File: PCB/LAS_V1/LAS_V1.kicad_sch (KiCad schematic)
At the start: 19 parts, among them J1 Screw_Terminal_01x04, J2 Conn_01x03_Pin, J3 Conn_01x05_Socket, J4 Conn_01x22_Socket, J5 Conn_01x22_Socket, SW1 SW_Push, SW2 SW_Push, U1 ESP32-S3-WROOM-1, U2 AMS1117-3.3

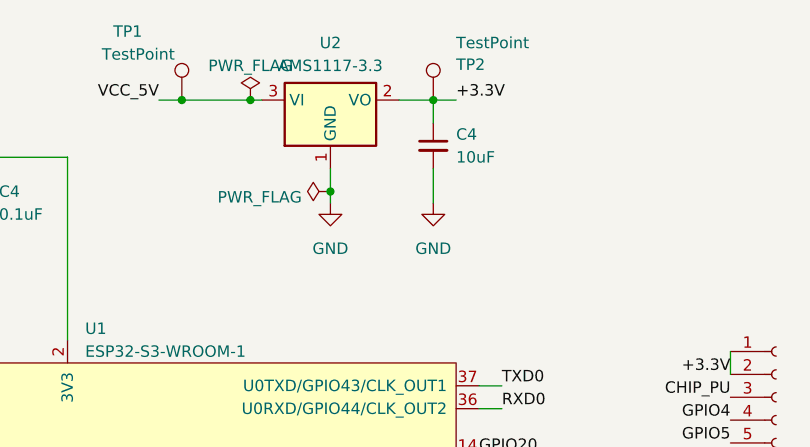
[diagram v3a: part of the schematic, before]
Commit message: All components Placed on PCB
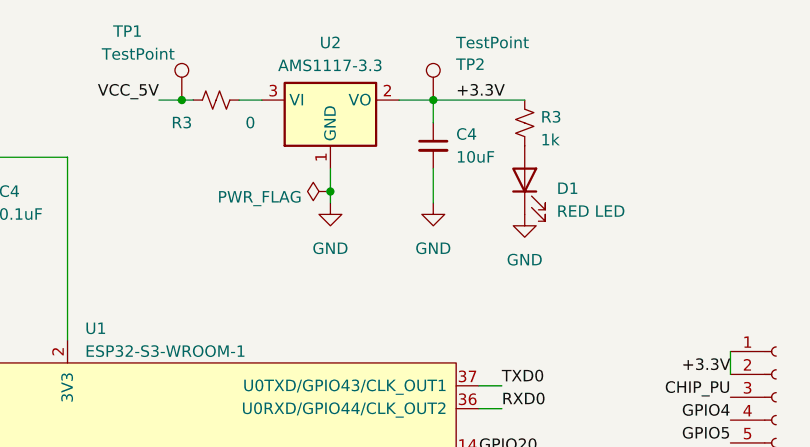
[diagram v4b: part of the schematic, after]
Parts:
- added D1: RED LED, LED_SMD:LED_0805_2012Metric, symbol Device:LED
- added R3: 1k, Resistor_SMD:R_0603_1608Metric, symbol Device:R_Small_US
- added R3: 0, Resistor_SMD:R_0603_1608Metric, symbol Device:R_Small_US
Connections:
- net +3.3V: now also R3.1
- net GND: now also D1.1 (K)
- net VCC_5V: now also R3.2; no longer U2.3 (VI)
- new net: D1.2 (A), R3.2
- new net: R3.1, U2.3 (VI)
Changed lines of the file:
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@@
   (junction (at 180.34 31.75) (diameter 0) (color 0 0 0 0)
-  )
-  (junction (at 210.82 25.4) (diameter 0) (color 0 0 0 0)
   )
   (junction (at 264.16 162.56) (diameter 0) (color 0 0 0 0)
@@
     (stroke (width 0) (type default))
   )
-  (wire (pts (xy 210.82 25.4) (xy 212.09 25.4))
+  (wire (pts (xy 203.2 25.4) (xy 204.47 25.4))
     (stroke (width 0) (type default))
   )
@@
     (stroke (width 0) (type default))
   )
-  (wire (pts (xy 203.2 25.4) (xy 210.82 25.4))
-    (stroke (width 0) (type default))
-  )
   (wire (pts (xy 160.02 148.59) (xy 160.02 147.32))
     (stroke (width 0) (type default))
   )
+  (wire (pts (xy 209.55 25.4) (xy 212.09 25.4))
+    (stroke (width 0) (type default))
+  )
   (wire (pts (xy 236.22 57.15) (xy 238.76 57.15))
     (stroke (width 0) (type default))
@@
     (stroke (width 0) (type default))
   )
-  (wire (pts (xy 231.14 25.4) (xy 233.68 25.4))
+  (wire (pts (xy 231.14 25.4) (xy 241.3 25.4))
     (stroke (width 0) (type default))
   )
@@
   (symbol (lib_id "power:GND") (at 264.16 162.56 270) (unit 1)
     (in_bom yes) (on_board yes) (dnp no) (fields_autoplaced)
-    (property "Reference" "#PWR014" (at 257.81 162.56 0)
+    (property "Reference" "#PWR015" (at 257.81 162.56 0)
       (effects (font (size 1.27 1.27)) hide)
     )
@@
       (project "LAS_V1"
         (path "/aadef4b8-3115-4a49-998f-828f2021a6b4"
-          (reference "#PWR014") (unit 1)
+          (reference "#PWR015") (unit 1)
         )
       )
@@
     )
   )
+  (symbol (lib_id "Device:R_Small_US") (at 241.3 27.94 0) (unit 1)
+    (in_bom yes) (on_board yes) (dnp no) (fields_autoplaced)
+    (property "Reference" "R3" (at 243.078 27.305 0)
+      (effects (font (size 1.27 1.27)) (justify left))
+    )
+    (property "Value" "1k" (at 243.078 29.845 0)
+      (effects (font (size 1.27 1.27)) (justify left))
+    )
+    (property "Footprint" "Resistor_SMD:R_0603_1608Metric" (at 241.3 27.94 0)
+      (effects (font (size 1.27 1.27)) hide)
+    )
+    (property "Datasheet" "~" (at 241.3 27.94 0)
+      (effects (font (size 1.27 1.27)) hide)
+    )
+    (property "LCSC" "C21190" (at 241.3 27.94 0)
+      (effects (font (size 1.27 1.27)) hide)
+    )
+    (pin "1")
+    (pin "2")
+    (instances
+      (project "LAS_V1"
+        (path "/aadef4b8-3115-4a49-998f-828f2021a6b4/f48c28f3-4e7e-4446-924c-0b87434ade9c"
+          (reference "R3") (unit 1)
+        )
+        (path "/aadef4b8-3115-4a49-998f-828f2021a6b4"
+          (reference "R4") (unit 1)
+        )
+      )
+    )
+  )
   (symbol (lib_id "power:GND") (at 149.86 149.86 0) (unit 1)
     (in_bom yes) (on_board yes) (dnp no) (fields_autoplaced)
@@
     )
   )
+  (symbol (lib_id "power:GND") (at 241.3 38.1 0) (unit 1)
+    (in_bom yes) (on_board yes) (dnp no) (fields_autoplaced)
+    (property "Reference" "#PWR013" (at 241.3 44.45 0)
+      (effects (font (size 1.27 1.27)) hide)
+    )
+    (property "Value" "GND" (at 241.3 43.18 0)
+      (effects (font (size 1.27 1.27)))
+    )
+    (property "Footprint" "" (at 241.3 38.1 0)
+      (effects (font (size 1.27 1.27)) hide)
+    )
+    (property "Datasheet" "" (at 241.3 38.1 0)
+      (effects (font (size 1.27 1.27)) hide)
+    )
+    (pin "1")
+    (instances
+      (project "LAS_V1"
+        (path "/aadef4b8-3115-4a49-998f-828f2021a6b4"
+          (reference "#PWR013") (unit 1)
+        )
+      )
+    )
+  )
   (symbol (lib_id "power:GND") (at 231.14 36.83 0) (unit 1)
     (in_bom yes) (on_board yes) (dnp no) (fields_autoplaced)
@@
         (path "/aadef4b8-3115-4a49-998f-828f2021a6b4"
           (reference "#PWR012") (unit 1)
+        )
+      )
+    )
+  )
+  (symbol (lib_id "Device:R_Small_US") (at 207.01 25.4 270) (unit 1)
+    (in_bom yes) (on_board yes) (dnp no)
+    (property "Reference" "R3" (at 203.2 27.94 90)
+      (effects (font (size 1.27 1.27)))
+    )
+    (property "Value" "0" (at 210.82 27.94 90)
+      (effects (font (size 1.27 1.27)))
+    )
+    (property "Footprint" "Resistor_SMD:R_0603_1608Metric" (at 207.01 25.4 0)
+      (effects (font (size 1.27 1.27)) hide)
+    )
+    (property "Datasheet" "~" (at 207.01 25.4 0)
+      (effects (font (size 1.27 1.27)) hide)
+    )
+    (pin "1")
+    (pin "2")
+    (instances
+      (project "LAS_V1"
+        (path "/aadef4b8-3115-4a49-998f-828f2021a6b4"
+          (reference "R3") (unit 1)
         )
       )
@@
         )
         (path "/aadef4b8-3115-4a49-998f-828f2021a6b4"
-          (reference "#FLG02") (unit 1)
+          (reference "#FLG01") (unit 1)
         )
       )
@@
     )
   )
-  (symbol (lib_id "power:PWR_FLAG") (at 210.82 25.4 0) (unit 1)
-    (in_bom yes) (on_board yes) (dnp no) (fields_autoplaced)
-    (property "Reference" "#FLG02" (at 210.82 23.495 0)
-      (effects (font (size 1.27 1.27)) hide)
-    )
-    (property "Value" "PWR_FLAG" (at 210.82 21.59 0)
-      (effects (font (size 1.27 1.27)))
-    )
-    (property "Footprint" "" (at 210.82 25.4 0)
-      (effects (font (size 1.27 1.27)) hide)
-    )
-    (property "Datasheet" "~" (at 210.82 25.4 0)
-      (effects (font (size 1.27 1.27)) hide)
-    )
-    (pin "1")
-    (instances
-      (project "LAS_V1"
-        (path "/aadef4b8-3115-4a49-998f-828f2021a6b4/a475df9f-c6e9-4f77-bf99-c031d1147f10"
-          (reference "#FLG02") (unit 1)
-        )
-        (path "/aadef4b8-3115-4a49-998f-828f2021a6b4"
-          (reference "#FLG01") (unit 1)
-        )
-      )
-    )
-  )
   (symbol (lib_id "Device:C_Small") (at 231.14 30.48 0) (unit 1)
     (in_bom yes) (on_board yes) (dnp no) (fields_autoplaced)
@@
     )
   )
+  (symbol (lib_id "Device:LED") (at 241.3 34.29 90) (unit 1)
+    (in_bom yes) (on_board yes) (dnp no) (fields_autoplaced)
+    (property "Reference" "D1" (at 244.856 35.2425 90)
+      (effects (font (size 1.27 1.27)) (justify right))
+    )
+    (property "Value" "RED LED" (at 244.856 37.7825 90)
+      (effects (font (size 1.27 1.27)) (justify right))
+    )
+    (property "Footprint" "LED_SMD:LED_0805_2012Metric" (at 241.3 34.29 0)
+      (effects (font (size 1.27 1.27)) hide)
+    )
+    (property "Datasheet" "~" (at 241.3 34.29 0)
+      (effects (font (size 1.27 1.27)) hide)
+    )
+    (property "LCSC" "C84256" (at 241.3 34.29 0)
+      (effects (font (size 1.27 1.27)) hide)
+    )
+    (pin "1")
+    (pin "2")
+    (instances
+      (project "LAS_V1"
+        (path "/aadef4b8-3115-4a49-998f-828f2021a6b4"
+          (reference "D1") (unit 1)
+        )
+        (path "/aadef4b8-3115-4a49-998f-828f2021a6b4/f48c28f3-4e7e-4446-924c-0b87434ade9c"
+          (reference "D1") (unit 1)
+        )
+      )
+    )
+  )
   (symbol (lib_id "Connector:Conn_01x03_Pin") (at 36.83 21.59 270) (unit 1)
     (in_bom yes) (on_board yes) (dnp no) (fields_autoplaced)
@@
   (symbol (lib_id "power:GND") (at 264.16 110.49 270) (unit 1)
     (in_bom yes) (on_board yes) (dnp no) (fields_autoplaced)
-    (property "Reference" "#PWR013" (at 257.81 110.49 0)
+    (property "Reference" "#PWR014" (at 257.81 110.49 0)
       (effects (font (size 1.27 1.27)) hide)
     )
@@
       (project "LAS_V1"
         (path "/aadef4b8-3115-4a49-998f-828f2021a6b4"
-          (reference "#PWR013") (unit 1)
-        )
-      )
+          (reference "#PWR014") (unit 1)
+        )
+      )

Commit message: PCB V1 complete
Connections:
- net LIVE: now also J1.3 (Pin_3); no longer J1.4 (Pin_4)
- net N01: now also J1.1 (Pin_1); no longer J1.2 (Pin_2)
- net NC1: now also J1.2 (Pin_2); no longer J1.3 (Pin_3)
- net NEUTRAL: now also J1.4 (Pin_4); no longer J1.1 (Pin_1)
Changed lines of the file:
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@@
     (stroke (width 0) (type default))
   )
-  (wire (pts (xy 44.45 54.61) (xy 34.29 54.61))
+  (wire (pts (xy 45.72 54.61) (xy 34.29 54.61))
     (stroke (width 0) (type default))
   )
@@
     (effects (font (size 1.27 1.27)) (justify right bottom))
   )
-  (label "NEUTRAL" (at 44.45 54.61 0) (fields_autoplaced)
+  (label "NEUTRAL" (at 44.45 46.99 0) (fields_autoplaced)
     (effects (font (size 1.27 1.27)) (justify left bottom))
   )
@@
     (effects (font (size 1.27 1.27)) (justify right bottom))
   )
+  (label "NC1" (at 45.72 52.07 0) (fields_autoplaced)
+    (effects (font (size 1.27 1.27)) (justify left bottom))
+  )
   (label "GPIO36" (at 264.16 138.43 180) (fields_autoplaced)
     (effects (font (size 1.27 1.27)) (justify right bottom))
@@
     (effects (font (size 1.27 1.27)) (justify right bottom))
   )
-  (label "NC1" (at 45.72 49.53 0) (fields_autoplaced)
-    (effects (font (size 1.27 1.27)) (justify left bottom))
-  )
   (label "GPIO42" (at 264.16 123.19 180) (fields_autoplaced)
     (effects (font (size 1.27 1.27)) (justify right bottom))
@@
     (effects (font (size 1.27 1.27)) (justify left bottom))
   )
+  (label "N01" (at 45.72 54.61 0) (fields_autoplaced)
+    (effects (font (size 1.27 1.27)) (justify left bottom))
+  )
   (label "NC1" (at 78.74 118.11 0) (fields_autoplaced)
     (effects (font (size 1.27 1.27)) (justify left bottom))
@@
     (effects (font (size 1.27 1.27)) (justify left bottom))
   )
-  (label "N01" (at 45.72 52.07 0) (fields_autoplaced)
-    (effects (font (size 1.27 1.27)) (justify left bottom))
-  )
-  (label "LIVE" (at 44.45 46.99 0) (fields_autoplaced)
-    (effects (font (size 1.27 1.27)) (justify left bottom))
-  )
   (label "GPIO6" (at 238.76 87.63 0) (fields_autoplaced)
     (effects (font (size 1.27 1.27)) (justify left bottom))
@@
     (effects (font (size 1.27 1.27)) (justify right bottom))
   )
+  (label "LIVE" (at 45.72 49.53 0) (fields_autoplaced)
+    (effects (font (size 1.27 1.27)) (justify left bottom))
+  )
   (label "GPIO12" (at 236.22 102.87 0) (fields_autoplaced)

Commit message: PCBV1 done, moving onto V2
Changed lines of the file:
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@@
-    (stroke (width 0) (type default))
-  )
-  (wire (pts (xy 243.84 80.01) (xy 236.22 80.01))
     (stroke (width 0) (type default))
   )
@@
     (stroke (width 0) (type default))
   )
-  (wire (pts (xy 245.11 120.65) (xy 236.22 120.65))
+  (wire (pts (xy 245.11 113.03) (xy 236.22 113.03))
     (stroke (width 0) (type default))
   )
@@
     (stroke (width 0) (type default))
   )
+  (wire (pts (xy 246.38 82.55) (xy 236.22 82.55))
+    (stroke (width 0) (type default))
+  )
   (wire (pts (xy 236.22 72.39) (xy 250.19 72.39))
     (stroke (width 0) (type default))
@@
     (effects (font (size 1.27 1.27)) (justify left bottom))
   )
-  (label "RX1" (at 245.11 120.65 0) (fields_autoplaced)
-    (effects (font (size 1.27 1.27)) (justify left bottom))
-  )
   (label "GPIO40" (at 264.16 128.27 180) (fields_autoplaced)
     (effects (font (size 1.27 1.27)) (justify right bottom))
@@
     (effects (font (size 1.27 1.27)) (justify left bottom))
   )
-  (label "LED_GREEN" (at 243.84 80.01 0) (fields_autoplaced)
-    (effects (font (size 1.27 1.27)) (justify left bottom))
-  )
   (label "GPIO15" (at 144.78 64.77 180) (fields_autoplaced)
     (effects (font (size 1.27 1.27)) (justify right bottom))
@@
     (effects (font (size 1.27 1.27)) (justify right bottom))
   )
+  (label "LED_GREEN" (at 246.38 82.55 0) (fields_autoplaced)
+    (effects (font (size 1.27 1.27)) (justify left bottom))
+  )
   (label "LED_RED" (at 243.84 74.93 0) (fields_autoplaced)
     (effects (font (size 1.27 1.27)) (justify left bottom))
@@
     (effects (font (size 1.27 1.27)) (justify right bottom))
   )
+  (label "RX1" (at 245.11 113.03 0) (fields_autoplaced)
+    (effects (font (size 1.27 1.27)) (justify left bottom))
+  )
   (label "GPIO12" (at 264.16 96.52 180) (fields_autoplaced)
